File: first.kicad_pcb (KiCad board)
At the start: 2 copper layers, 100 x 100 mm, 52 parts, among them J1 Conn_01x02_Socket, J10 Conn_01x02_Socket, J11 USB_C_Receptacle_USB2.0_16P, J12 Conn_01x03_Socket, J2 Conn_01x03_Socket, J3 Conn_01x03_Socket, J4 Conn_01x03_Socket, J5 Conn_01x03_Socket, J6 Conn_01x03_Socket, J7 Conn_01x03_Socket, J8 Conn_01x03_Socket, J9 Conn_01x03_Socket, SW1 SW_Push, SW3 SW_Wuerth_450301014042, U1 STM32F446RETx, U2 MCP2561-E-SN, U3 CH340E, U4 BD33FC0FP, U5 BD50FC0FP

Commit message: 次のコミット時に記入
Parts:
- moved C2 1.27 mm to (91.9, 107.2)
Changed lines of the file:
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@@
 	(footprint "Capacitor_SMD:C_0603_1608Metric_Pad1.08x0.95mm_HandSolder"
 		(layer "F.Cu")
-		(at 91.91 108.42 180)
+		(at 91.91 107.15 180)
 		(descr "Capacitor SMD 0603 (1608 Metric), square (rectangular) end terminal, IPC-7351 nominal with elongated pad for handsoldering. (Body size source: IPC-SM-782 page 76, https://www.pcb-3d.com/wordpress/wp-content/uploads/ipc-sm-782a_amendment_1_and_2.pdf), generated with kicad-footprint-generator")
 		(tags "capacitor handsolder")

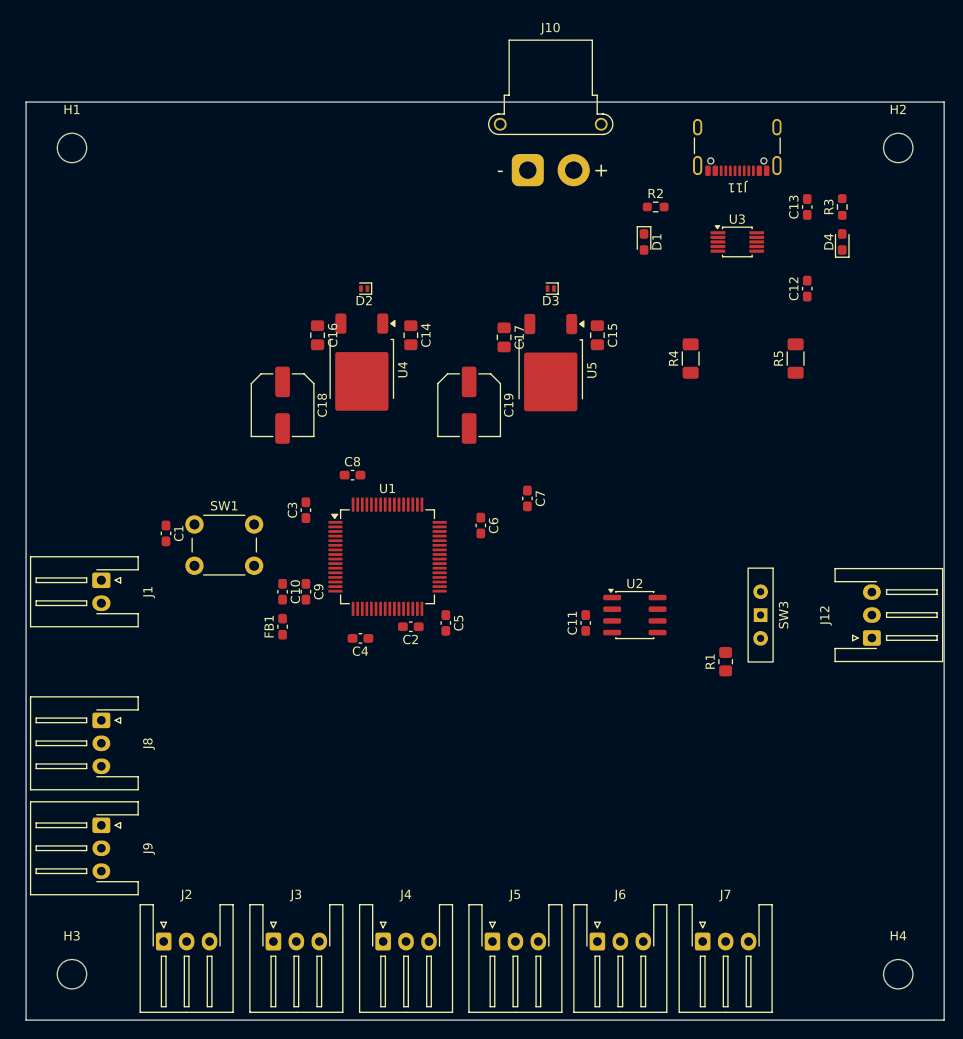
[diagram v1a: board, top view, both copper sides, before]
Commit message: 回路図の一部素子の変更、削除。pcbの電源回りの配線
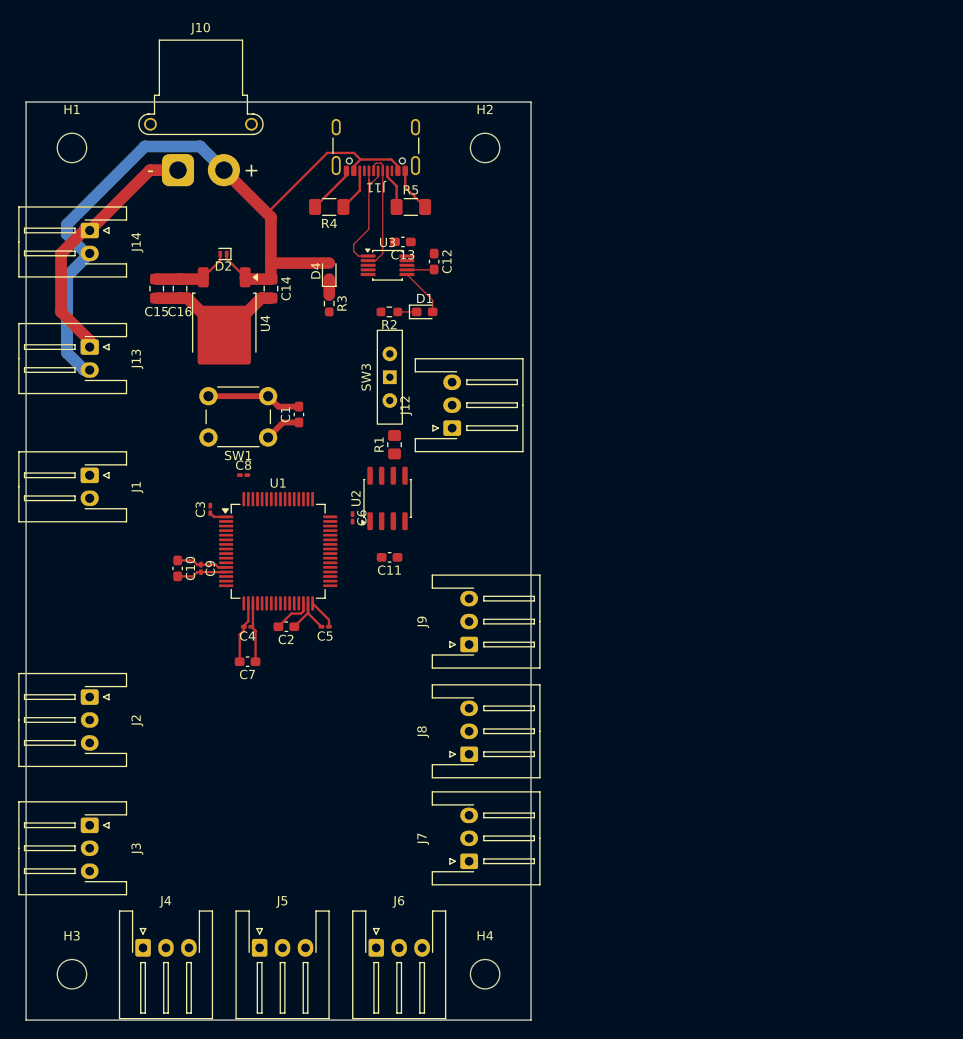
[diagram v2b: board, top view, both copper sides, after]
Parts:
- removed C17: 4.7μF, Capacitor_SMD:C_0805_2012Metric_Pad1.18x1.45mm_HandSolder
- removed C18, C19: C_Polarized, Capacitor_SMD:C_Elec_6.3x7.7
- removed D3: D_Shockley, Diode_SMD:D_SOD-882
- removed FB1: FerriteBead, Inductor_SMD:L_0603_1608Metric_Pad1.05x0.95mm_HandSolder
- removed U5: BD50FC0FP, Package_TO_SOT_SMD:TO-252-2
- added J13: Conn_01x02_Socket, Connector_JST:JST_XH_S2B-XH-A-1_1x02_P2.50mm_Horizontal, F.Cu at (56.9, 76.7)
- added J14: Conn_01x02_Socket, Connector_JST:JST_XH_S2B-XH-A-1_1x02_P2.50mm_Horizontal, F.Cu at (56.9, 64.0)
- C15: value 4.7μF -> 22μF
- C2: value 2.2μF -> 4.7μF
- C3, C4, C5, C6, C8, C9: footprint Capacitor_SMD:C_0603_1608Metric_Pad1.08x0.95mm_HandSolder -> Capacitor_SMD:C_0201_0603Metric_Pad0.64x0.40mm_HandSolder
- D1: value LED_RED -> LED_GREEN
- D4: value LED_GREEN -> LED_RED
- moved R3 56.9 mm to (83.0, 71.9), turned to -90 degrees
- moved D4 56.0 mm to (83.0, 68.4)
- moved J12 51.1 mm to (96.4, 85.5)
- moved C15 48.3 mm to (64.2, 70.3)
- moved SW3 48.0 mm to (89.6, 80.0)
- moved R5 45.0 mm to (91.9, 61.4), turned to 0 degrees
- moved H2 45.0 mm to (100.0, 55.0)
- moved H4 45.0 mm to (100.0, 145.0)
- moved J9 44.6 mm to (98.3, 109.1), turned to 90 degrees
- moved C13 44.2 mm to (91.0, 65.2), turned to 180 degrees
- moved R1 43.1 mm to (90.1, 87.3)
- moved R4 42.7 mm to (83.0, 61.4), turned to 180 degrees
- moved C12 40.7 mm to (94.5, 67.4), turned to -90 degrees
- moved J8 40.2 mm to (98.3, 121.0), turned to 90 degrees
- moved J11 39.4 mm to (88.1, 53.8)
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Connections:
- C10 pad 2: Net-(U1-VDDA) -> +3.3V
- C14 pad 1: VCC -> +5V
- C15 pad 1: VCC -> +3.3V
- C9 pad 2: Net-(U1-VDDA) -> +3.3V
- D2 pad 1: VCC -> +5V
- J10 pad 2: VCC -> +5V
- U1 pad 13: Net-(U1-VDDA) -> +3.3V
- U4 pad 1: VCC -> +5V
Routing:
- net +5V: track 0.00 -> 90.7 mm
- net GND: track 0.00 -> 82.9 mm
- net +3.3V: track 0.00 -> 25.7 mm
- net D-: track 0.00 -> 13.3 mm
- net D+: track 0.00 -> 13.2 mm
- net Net-(D1-A): track 0.00 -> 5.24 mm
- net Net-(J11-CC2): track 0.00 -> 4.68 mm
- net Net-(J11-CC1): track 0.00 -> 4.36 mm
- net Net-(U1-VCAP_1): track 0.00 -> 4.27 mm
- net Net-(U1-NRST): track 0.00 -> 4.03 mm
- net Net-(D1-K): track 0.00 -> 2.06 mm
- net Net-(D4-K): track 0.00 -> 1.74 mm
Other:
- board size 100 x 100 mm -> 55 x 100 mm

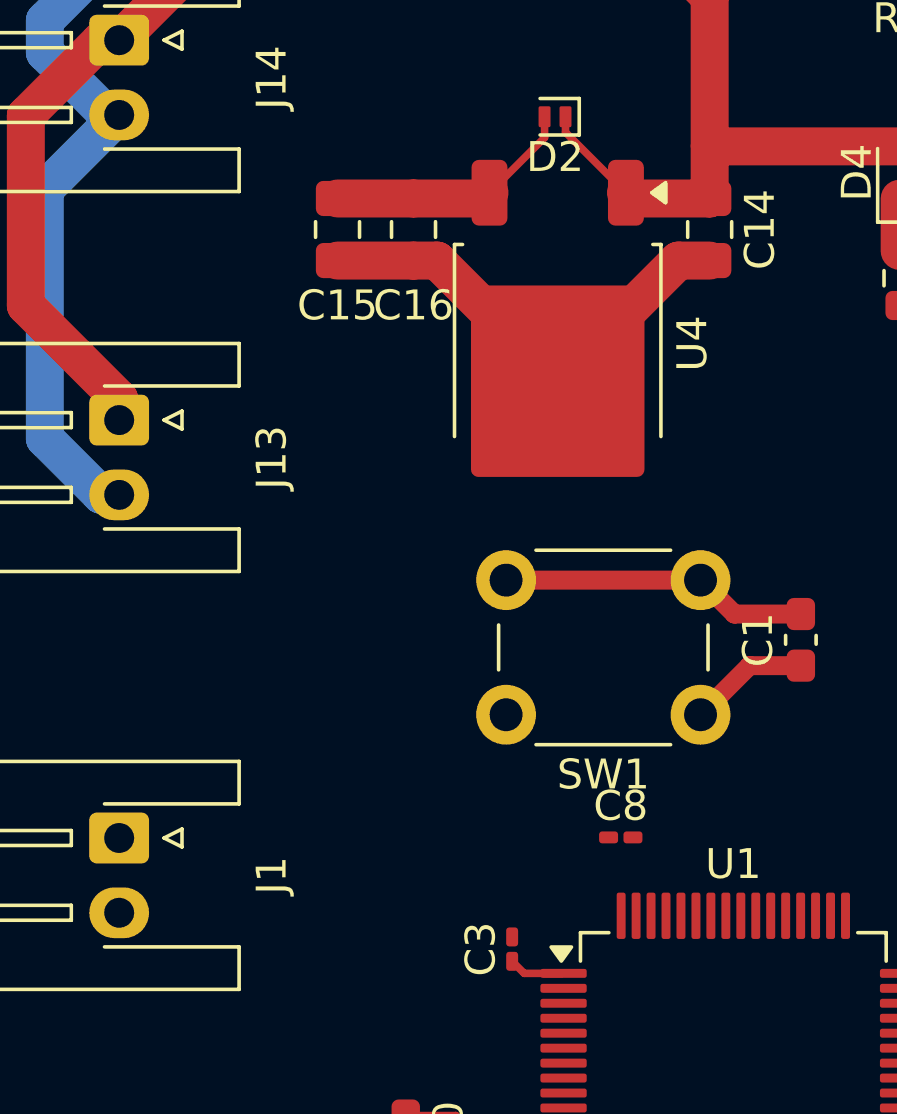
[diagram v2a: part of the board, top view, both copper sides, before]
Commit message: 電源回りの配線の改良(third.pcbの元ファイル)
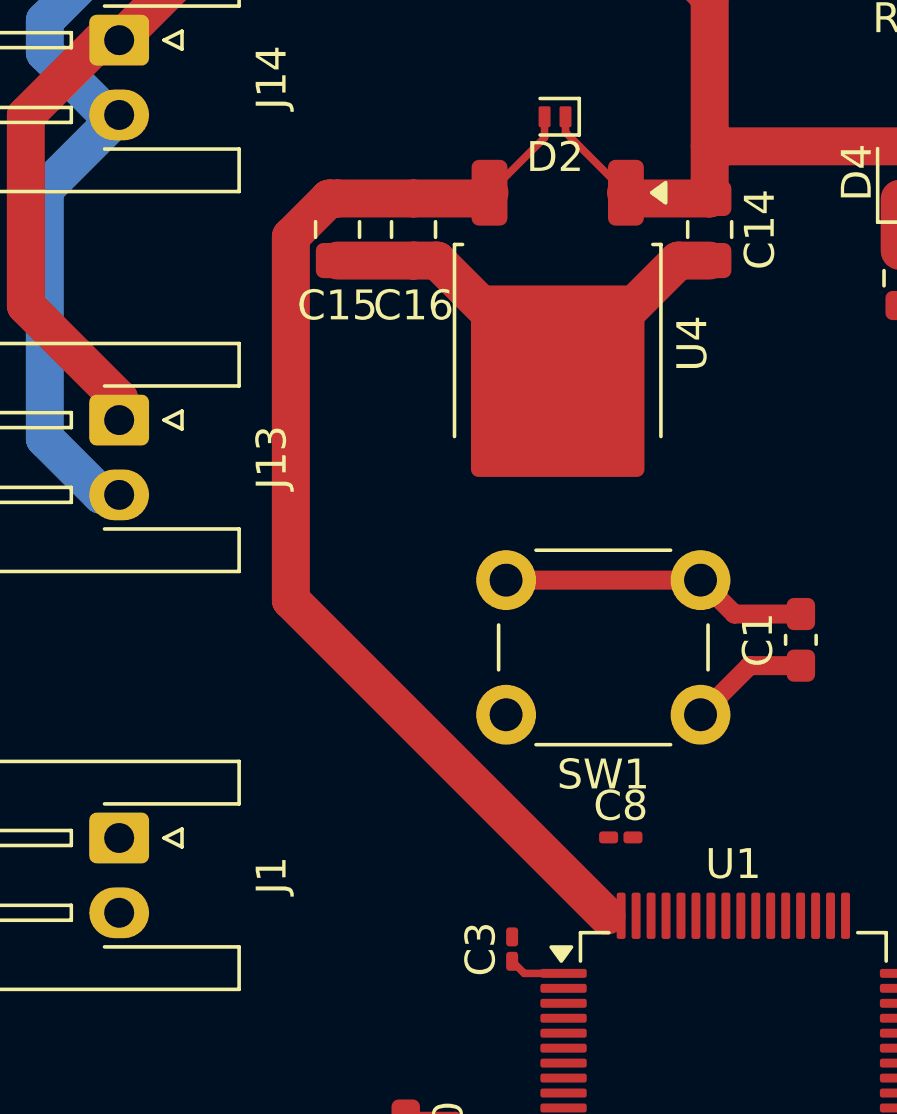
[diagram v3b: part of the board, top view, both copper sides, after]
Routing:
- net +3.3V: track 25.7 -> 54.9 mm
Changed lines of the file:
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@@
+	)
+	(segment
+		(start 62.669 82.705)
+		(end 73.224 93.26)
+		(width 1.27)
+		(layer "F.Cu")
+		(net 9)
 	)
 	(segment
@@
 		(end 70.469 95.185)
 		(width 0.254)
+		(layer "F.Cu")
+		(net 9)
+	)
+	(segment
+		(start 63.949738 69.2825)
+		(end 62.669 70.563238)
+		(width 1.27)
 		(layer "F.Cu")
 		(net 9)
@@
 	)
 	(segment
+		(start 64.23 69.2825)
+		(end 63.949738 69.2825)
+		(width 1.27)
+		(layer "F.Cu")
+		(net 9)
+	)
+	(segment
 		(start 66.77 69.2825)
 		(end 64.23 69.2825)
 		(width 1.27)
 		(layer "F.Cu")
+		(net 9)
+	)
+	(segment
+		(start 62.669 70.563238)
+		(end 62.669 82.705)
+		(width 1.27)
+		(layer "F.Cu")

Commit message: autoroutingで全体を配線した
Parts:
- moved C8 1.06 mm to (74.0, 91.7)
- moved C7 0.96 mm to (74.1, 110.0)
- moved C6 0.82 mm to (84.8, 95.6)
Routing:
- net GND: track 82.9 -> 32.9 mm
- net +3.3V: track 54.9 -> 57.2 mm
- added copper zone on B.Cu, net GND
- added copper zone on F.Cu, net GND
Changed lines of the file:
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@@
 	(footprint "Capacitor_SMD:C_0201_0603Metric_Pad0.64x0.40mm_HandSolder"
 		(layer "F.Cu")
-		(at 85.56 95.2875 -90)
+		(at 84.798 95.593 -90)
 		(descr "Capacitor SMD 0201 (0603 Metric), square (rectangular) end terminal, IPC-7351 nominal with elongated pad for handsoldering. (Body size source: https://www.vishay.com/docs/20052/crcw0201e3.pdf), generated with kicad-footprint-generator")
 		(tags "capacitor handsolder")
@@
 	(footprint "Capacitor_SMD:C_0201_0603Metric_Pad0.64x0.40mm_HandSolder"
 		(layer "F.Cu")
-		(at 73.6975 90.64)
+		(at 74.003 91.656)
 		(descr "Capacitor SMD 0201 (0603 Metric), square (rectangular) end terminal, IPC-7351 nominal with elongated pad for handsoldering. (Body size source: https://www.vishay.com/docs/20052/crcw0201e3.pdf), generated with kicad-footprint-generator")
 		(tags "capacitor handsolder")
@@
 	(footprint "Capacitor_SMD:C_0603_1608Metric_Pad1.08x0.95mm_HandSolder"
 		(layer "F.Cu")
-		(at 74.13 110.96 180)
+		(at 74.13 110 180)
 		(descr "Capacitor SMD 0603 (1608 Metric), square (rectangular) end terminal, IPC-7351 nominal with elongated pad for handsoldering. (Body size source: IPC-SM-782 page 76, https://www.pcb-3d.com/wordpress/wp-content/uploads/ipc-sm-782a_amendment_1_and_2.pdf), generated with kicad-footprint-generator")
 		(tags "capacitor handsolder")
@@
 	)
 	(segment
-		(start 70.937992 100.685)
-		(end 71.785 100.685)
-		(width 0.254)
-		(layer "F.Cu")
-		(net 1)
-	)
-	(segment
 		(start 76.67 71.3575)
 		(end 75.6225 71.3575)
@@
 	)
 	(segment
-		(start 70.645492 100.3925)
-		(end 70.937992 100.685)
-		(width 0.254)
-		(layer "F.Cu")
-		(net 1)
-	)
-	(segment
-		(start 73.7225 107.15)
-		(end 73.7225 107.5575)
-		(width 0.254)
-		(layer "F.Cu")
-		(net 1)
-	)
-	(segment
-		(start 80.71 105.68)
-		(end 82.18 107.15)
-		(width 0.254)
-		(layer "F.Cu")
-		(net 1)
-	)
-	(segment
 		(start 67.5575 71.3575)
 		(end 71.59 75.39)
@@
 	)
 	(segment
-		(start 80.71 104.61)
-		(end 80.71 105.68)
-		(width 0.254)
-		(layer "F.Cu")
-		(net 1)
-	)
-	(segment
 		(start 66.77 71.3575)
 		(end 67.5575 71.3575)
@@
 	)
 	(segment
-		(start 66.55 57.42)
-		(end 63.5 57.42)
-		(width 1.27)
-		(layer "F.Cu")
-		(net 1)
-	)
-	(segment
-		(start 91.3 59.27)
-		(end 93.46 61.43)
-		(width 0.254)
-		(layer "F.Cu")
-		(net 1)
-	)
-	(segment
 		(start 77.4975 83.1735)
 		(end 76.364 82.04)
@@
 	)
 	(segment
-		(start 73.7225 107.5575)
-		(end 73.2675 108.0125)
-		(width 0.254)
-		(layer "F.Cu")
-		(net 1)
-	)
-	(segment
-		(start 80.71 104.61)
-		(end 80.71 105.65)
-		(width 0.254)
-		(layer "F.Cu")
-		(net 1)
-	)
-	(segment
 		(start 84.9 57.49)
 		(end 84.9 58)
@@
 	)
 	(segment
-		(start 74.21 106.551946)
-		(end 73.7225 107.039446)
-		(width 0.254)
-		(layer "F.Cu")
-		(net 1)
-	)
-	(segment
-		(start 56.33 63.99)
-		(end 53.81 66.51)
-		(width 1.27)
-		(layer "F.Cu")
-		(net 1)
-	)
-	(segment
-		(start 69.05 100.3925)
-		(end 68.6425 100.3925)
-		(width 0.254)
-		(layer "F.Cu")
-		(net 1)
-	)
-	(segment
-		(start 73.2675 108.0125)
-		(end 73.2675 110.96)
-		(width 0.254)
-		(layer "F.Cu")
-		(net 1)
-	)
-	(segment
 		(start 64.23 71.3575)
 		(end 66.77 71.3575)
@@
 	)
 	(segment
-		(start 63.5 57.42)
-		(end 56.93 63.99)
-		(width 1.27)
-		(layer "F.Cu")
-		(net 1)
-	)
-	(segment
-		(start 68.1875 99.9375)
-		(end 66.51 99.9375)
-		(width 0.254)
-		(layer "F.Cu")
-		(net 1)
-	)
-	(segment
-		(start 91.3 59.27)
-		(end 91.3 57.49)
-		(width 0.254)
-		(layer "F.Cu")
-		(net 1)
-	)
-	(segment
-		(start 74.21 104.61)
-		(end 74.21 106.551946)
-		(width 0.254)
-		(layer "F.Cu")
-		(net 1)
-	)
-	(segment
-		(start 80.71 105.65)
-		(end 79.21 107.15)
-		(width 0.254)
-		(layer "F.Cu")
-		(net 1)
-	)
-	(segment
-		(start 69.05 100.3925)
-		(end 70.645492 100.3925)
-		(width 0.254)
-		(layer "F.Cu")
-		(net 1)
-	)
-	(segment
 		(start 56.93 63.99)
 		(end 56.33 63.99)
@@
 	)
 	(segment
-		(start 53.81 66.51)
-		(end 53.81 72.86)
-		(width 1.27)
-		(layer "F.Cu")
-		(net 1)
-	)
-	(segment
 		(start 76.364 82.04)
 		(end 69.864 82.04)
@@
 	)
 	(segment
-		(start 53.81 72.86)
-		(end 56.93 75.98)
-		(width 1.27)
-		(layer "F.Cu")
-		(net 1)
-	)
-	(segment
-		(start 68.6425 100.3925)
-		(end 68.1875 99.9375)
-		(width 0.254)
-		(layer "F.Cu")
-		(net 1)
-	)
-	(segment
 		(start 89.35 58.137008)
 		(end 90.36 59.147008)
@@
 	)
 	(segment
+		(start 74.71 106.9775)
+		(end 74.5375 107.15)
+		(width 0.2)
+		(layer "F.Cu")
+		(net 9)
+	)
+	(segment
+		(start 74.71 104.61)
+		(end 74.71 106.9775)
+		(width 0.2)
+		(layer "F.Cu")
+		(net 9)
+	)
+	(segment
+		(start 74.9925 107.605)
+		(end 74.9925 110)
+		(width 0.2)
+		(layer "F.Cu")
+		(net 9)
+	)
+	(segment
 		(start 69.05 101.2075)
 		(end 71.7625 101.2075)
@@
 	)
 	(segment
-		(start 74.9925 107.605)
-		(end 74.9925 110.96)
-		(width 0.254)
+		(start 73.5955 91.656)
+		(end 73.5955 93.1455)
+		(width 0.2)
 		(layer "F.Cu")
 		(net 9)
 	)
 	(segment
-		(start 74.5375 107.15)
-		(end 74.9925 107.605)
+		(start 82.995 106.395)
+		(end 82.995 107.15)
 		(width 0.254)
 		(layer "F.Cu")
@@
 	)
 	(segment
-		(start 82.995 106.395)
-		(end 82.995 107.15)
-		(width 0.254)
+		(start 73.5955 93.1455)
+		(end 73.71 93.26)
+		(width 0.2)
 		(layer "F.Cu")
 		(net 9)
@@
 	)
 	(segment
+		(start 74.5375 107.15)
+		(end 74.9925 107.605)
+		(width 0.2)
+		(layer "F.Cu")
+		(net 9)
+	)
+	(segment
 		(start 71.7625 101.2075)
 		(end 71.785 101.185)
@@
 	)
 	(segment
-		(start 74.71 106.9775)
-		(end 74.5375 107.15)
-		(width 0.254)
+		(start 64.23 69.2825)
+		(end 63.949738 69.2825)
+		(width 1.27)
 		(layer "F.Cu")
 		(net 9)
 	)
 	(segment
-		(start 74.71 104.61)
-		(end 74.71 106.9775)
-		(width 0.254)
+		(start 84.7975 95.185)
+		(end 84.798 95.1855)
+		(width 0.2)
 		(layer "F.Cu")
 		(net 9)
 	)
 	(segment
-		(start 64.23 69.2825)
-		(end 63.949738 69.2825)
+		(start 66.77 69.2825)
+		(end 64.23 69.2825)
 		(width 1.27)
 		(layer "F.Cu")
@@
 	)
 	(segment
-		(start 66.77 69.2825)
-		(end 64.23 69.2825)
-		(width 1.27)
+		(start 83.135 95.185)
+		(end 84.7975 95.185)
+		(width 0.2)
 		(layer "F.Cu")
 		(net 9)
@@
 	)
 	(segment
-		(start 79.954008 105.713)
-		(end 80.21 105.457008)
-		(width 0.254)
+		(start 80.21 105.418824)
+		(end 80.21 104.61)
+		(width 0.2)
 		(layer "F.Cu")
 		(net 30)
 	)
 	(segment
-		(start 80.21 105.457008)
-		(end 80.21 104.61)
-		(width 0.254)
+		(start 77.485 107.15)
+		(end 78.949 105.686)
+		(width 0.2)
 		(layer "F.Cu")
 		(net 30)
 	)
 	(segment
-		(start 78.922 105.713)
-		(end 79.954008 105.713)
-		(width 0.254)
+		(start 79.942824 105.686)
+		(end 80.21 105.418824)
+		(width 0.2)
 		(layer "F.Cu")
 		(net 30)
 	)
 	(segment
-		(start 77.485 107.15)
-		(end 78.922 105.713)
-		(width 0.254)
+		(start 78.949 105.686)
+		(end 79.942824 105.686)
+		(width 0.2)
 		(layer "F.Cu")
 		(net 30)
@@
 		(net 59)
 	)
+	(zone
+		(net 1)
+		(net_name "GND")
+		(layers "F.Cu" "B.Cu")
+		(hatch edge 0.5)
+		(connect_pads
+			(clearance 0.5)
+		)
+		(min_thickness 0.25)
+		(filled_areas_thickness no)
+		(fill yes
+			(thermal_gap 0.5)
+			(thermal_bridge_width 0.5)
+		)
+		(polygon
+			(pts
+				(xy 51 51) (xy 104 51) (xy 104 149) (xy 51 149)
+			)
+		)
+	)
 	(embedded_fonts no)
